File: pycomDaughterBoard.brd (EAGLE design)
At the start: 42.9 x 43.2 mm, 15 parts, among them J2 VCC

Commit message: Moved vias
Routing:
- net P9: track 21.1 -> 23.8 mm
- net P13: track 19.0 -> 20.4 mm
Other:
- board text added: "DS18 DATA"
- board text removed: "DS18B20 DATA"
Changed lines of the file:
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@@
 <text x="35.179" y="0.889" size="0.6096" layer="25" font="vector" ratio="20" rot="R180">P11</text>
 <text x="37.719" y="0.889" size="0.6096" layer="25" font="vector" ratio="20" rot="R180">P12</text>
-<text x="36.068" y="8.001" size="0.6096" layer="25" font="vector" ratio="20">BILGE
+<text x="36.068" y="8.128" size="0.6096" layer="25" font="vector" ratio="20">BILGE
 SWITCH</text>
 <text x="38.608" y="7.239" size="0.6096" layer="25" font="vector" ratio="20" rot="R270">LED</text>
-<text x="35.306" y="13.208" size="0.6096" layer="25" font="vector" ratio="20">DS18B20
+<text x="37.084" y="13.208" size="0.6096" layer="25" font="vector" ratio="20">DS18
 DATA</text>
-<text x="35.687" y="11.176" size="0.6096" layer="25" font="vector" ratio="20">BUTTON</text>
+<text x="35.941" y="11.176" size="0.6096" layer="25" font="vector" ratio="20">BUTTON</text>
 <text x="38.608" y="17.399" size="0.6096" layer="25" font="vector" ratio="20" rot="R270">3V3</text>
-<text x="38.481" y="19.939" size="0.6096" layer="25" font="vector" ratio="20" rot="R270">3V3</text>
-<text x="38.481" y="22.479" size="0.6096" layer="25" font="vector" ratio="20" rot="R270">GND</text>
-<text x="38.481" y="25.146" size="0.6096" layer="25" font="vector" ratio="20" rot="R270">GND</text>
+<text x="38.608" y="20.066" size="0.6096" layer="25" font="vector" ratio="20" rot="R270">3V3</text>
+<text x="38.608" y="22.479" size="0.6096" layer="25" font="vector" ratio="20" rot="R270">GND</text>
+<text x="38.608" y="24.892" size="0.6096" layer="25" font="vector" ratio="20" rot="R270">GND</text>
 <text x="9.144" y="11.938" size="0.6096" layer="25" font="vector" ratio="20" rot="R180">GND</text>
 <text x="9.144" y="14.097" size="0.6096" layer="25" font="vector" ratio="20" rot="R180">+5V</text>
@@
 <wire x1="29.21" y1="6.35" x2="29.21" y2="2.54" width="0.6096" layer="1"/>
 <wire x1="37.211" y1="13.97" x2="40.64" y2="13.97" width="0.6096" layer="1"/>
-<wire x1="36.957" y1="14.224" x2="37.211" y2="13.97" width="0.6096" layer="1"/>
-<wire x1="35.433" y1="12.7" x2="36.957" y2="14.224" width="0.6096" layer="16"/>
-<wire x1="31.496" y1="12.7" x2="35.433" y2="12.7" width="0.6096" layer="1"/>
+<wire x1="35.687" y1="15.494" x2="37.211" y2="13.97" width="0.6096" layer="1"/>
+<wire x1="31.496" y1="15.494" x2="35.687" y2="15.494" width="0.6096" layer="16"/>
+<wire x1="31.496" y1="12.7" x2="31.496" y2="15.494" width="0.6096" layer="1"/>
 <wire x1="29.083" y1="10.287" x2="31.496" y2="12.7" width="0.6096" layer="1"/>
 <wire x1="29.083" y1="6.604" x2="29.083" y2="10.287" width="0.6096" layer="1"/>
 <wire x1="29.083" y1="6.604" x2="29.21" y2="6.35" width="0.6096" layer="1"/>
-<via x="36.957" y="14.224" extent="1-16" drill="0.6096"/>
-<via x="35.433" y="12.7" extent="1-16" drill="0.6096"/>
+<via x="35.687" y="15.494" extent="1-16" drill="0.6096"/>
+<via x="31.496" y="15.494" extent="1-16" drill="0.6096"/>
 </signal>
 <signal name="P10" class="1">
@@
 <wire x1="36.83" y1="24.13" x2="36.83" y2="20.32" width="0.6096" layer="1"/>
 <wire x1="39.243" y1="8.89" x2="40.64" y2="8.89" width="0.6096" layer="1"/>
-<wire x1="36.449" y1="11.684" x2="39.243" y2="8.89" width="0.6096" layer="1"/>
-<wire x1="36.449" y1="12.192" x2="36.449" y2="11.684" width="0.6096" layer="16"/>
-<wire x1="38.1" y1="13.843" x2="36.449" y2="12.192" width="0.6096" layer="16"/>
-<wire x1="38.1" y1="15.113" x2="38.1" y2="13.843" width="0.6096" layer="16"/>
-<wire x1="38.1" y1="18.923" x2="38.1" y2="15.113" width="0.6096" layer="1"/>
-<wire x1="36.957" y1="20.066" x2="38.1" y2="18.923" width="0.6096" layer="1"/>
+<wire x1="34.417" y1="12.954" x2="39.243" y2="8.89" width="0.6096" layer="1"/>
+<wire x1="36.703" y1="13.97" x2="34.417" y2="12.954" width="0.6096" layer="16"/>
+<wire x1="36.957" y1="15.875" x2="36.703" y2="13.97" width="0.6096" layer="16"/>
+<wire x1="36.957" y1="16.256" x2="36.957" y2="15.875" width="0.6096" layer="16"/>
+<wire x1="36.957" y1="20.066" x2="36.957" y2="16.256" width="0.6096" layer="1"/>
 <wire x1="36.957" y1="20.066" x2="36.83" y2="20.32" width="0.6096" layer="1"/>
-<via x="36.449" y="11.684" extent="1-16" drill="0.6096"/>
-<via x="38.1" y="15.113" extent="1-16" drill="0.6096"/>
+<via x="34.417" y="12.954" extent="1-16" drill="0.6096"/>
+<via x="36.957" y="16.256" extent="1-16" drill="0.6096"/>
 </signal>
 <signal name="P16" class="1">

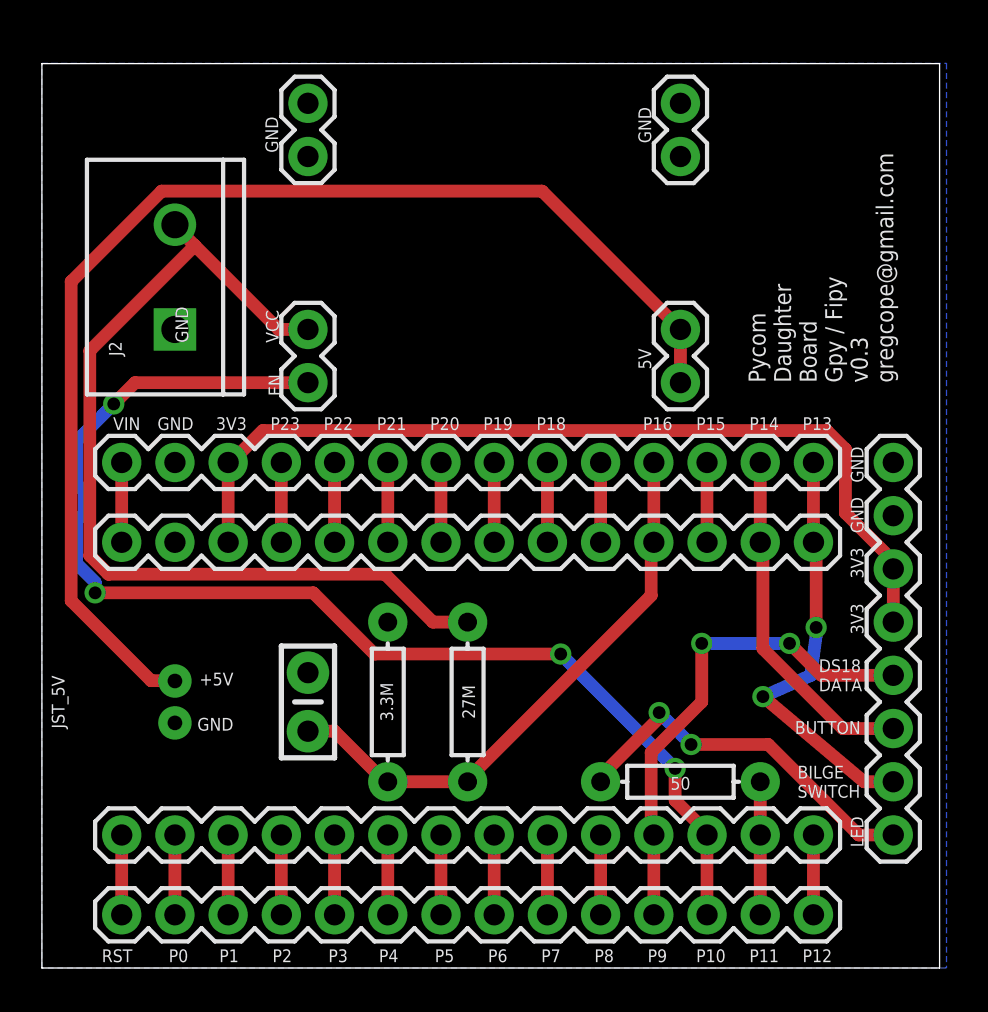
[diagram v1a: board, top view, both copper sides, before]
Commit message: Text update, move VCC connector
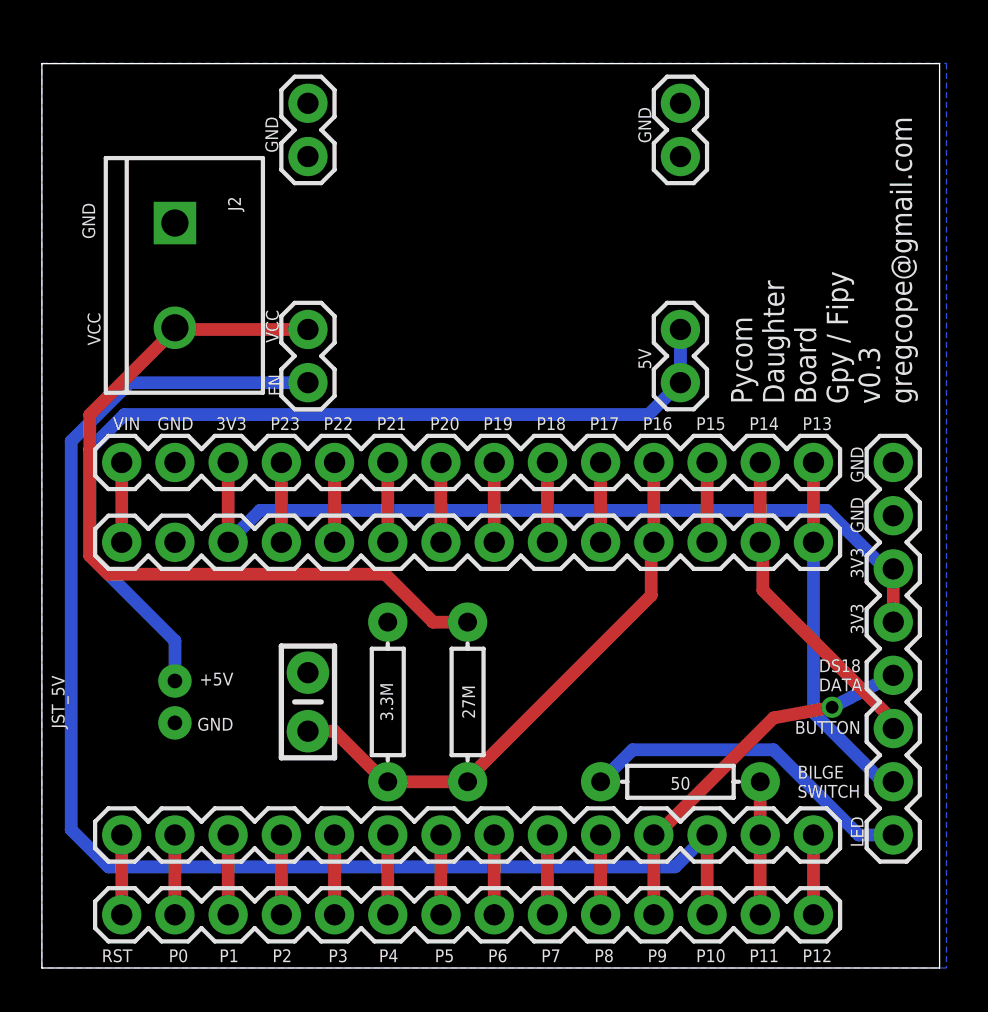
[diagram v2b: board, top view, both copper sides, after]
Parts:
- moved J2 5.08 mm to (6.35, 35.6), turned to 270 degrees
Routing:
- net 5V: track 57.9 -> 44.8 mm
- net P10: track 58.9 -> 66.5 mm, vias 4 -> 0
- net VCC: track 44.7 -> 38.3 mm
- net P9: track 23.8 -> 18.0 mm, vias 2 -> 1
- net 3V3: track 43.4 -> 39.9 mm
- net P13: track 20.4 -> 17.1 mm, vias 2 -> 0
- net N$2: track 18.1 -> 16.3 mm, vias 2 -> 0
- net P14: track 16.7 -> 15.3 mm
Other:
- board text added: "P17"
- board text added: "VCC"
